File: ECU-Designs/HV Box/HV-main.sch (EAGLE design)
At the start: 57 parts, among them IC2 MCP6002, IC3 MCP6002, T1 120, T2 120

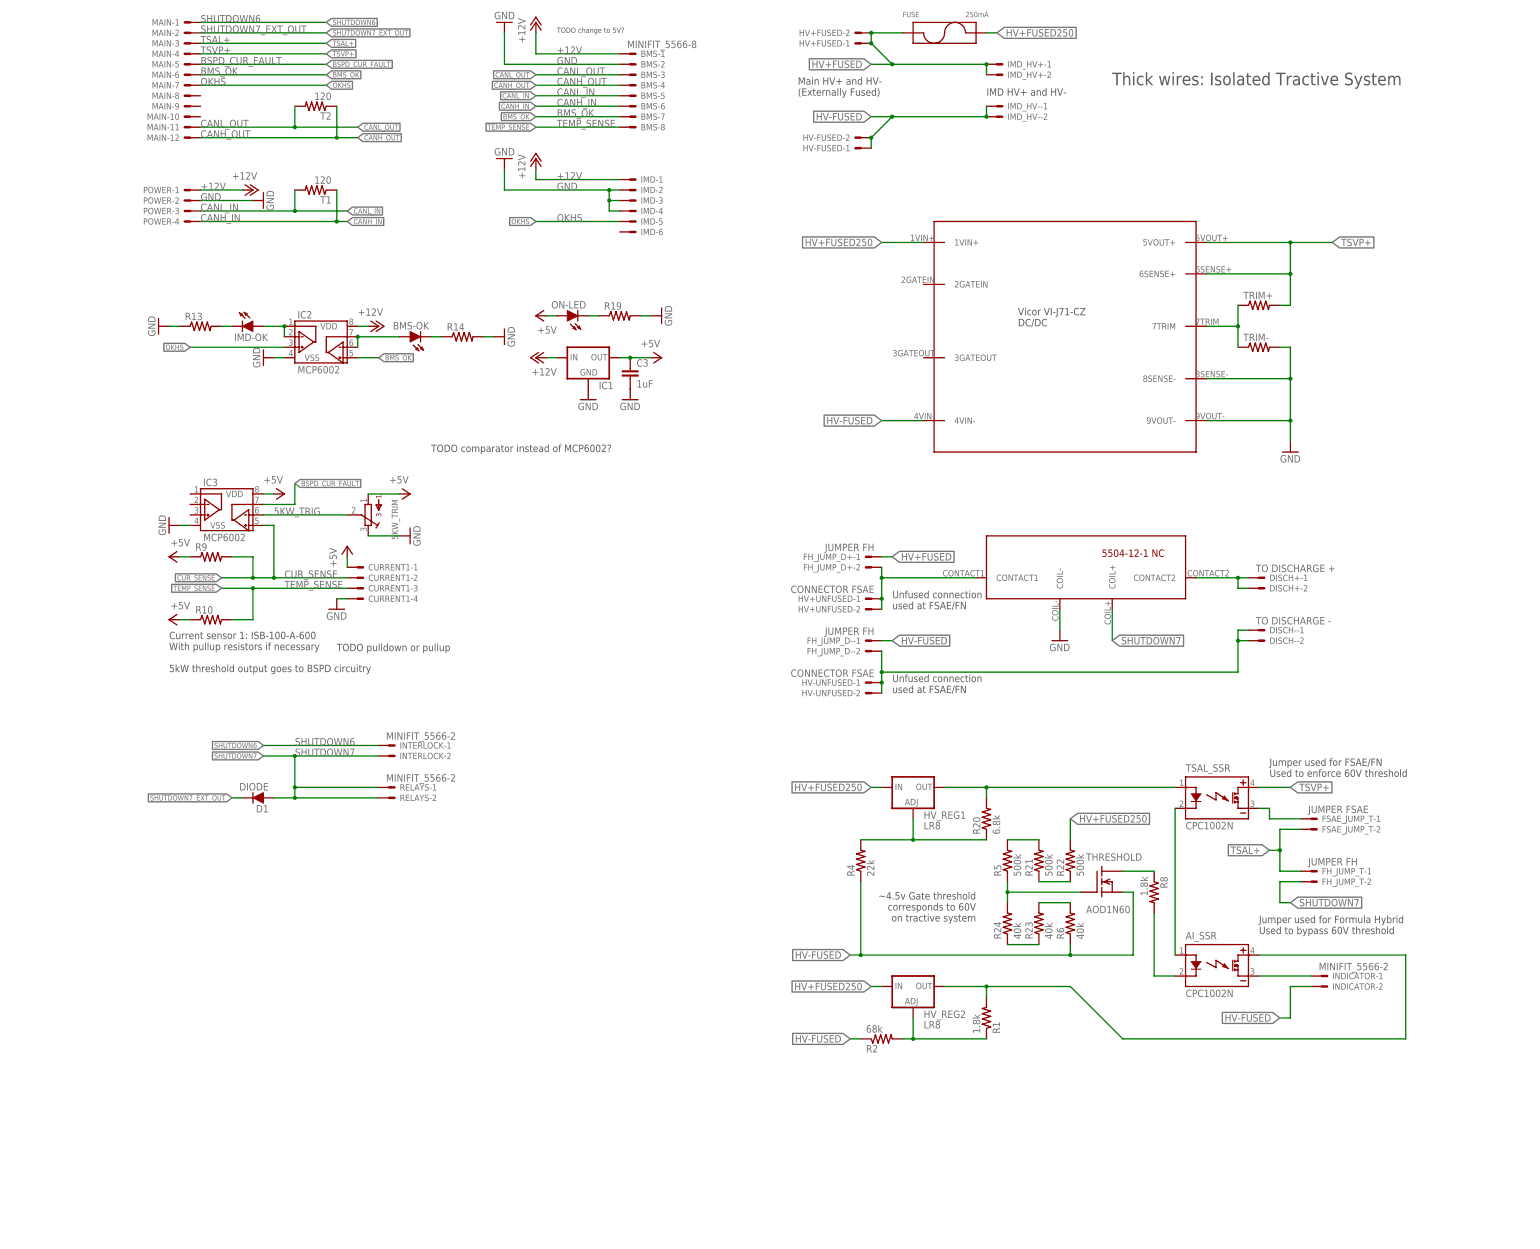
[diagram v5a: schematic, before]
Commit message: Change BSPD to use MCP6002 as comparator, HV board more resistors to meet voltage ratings
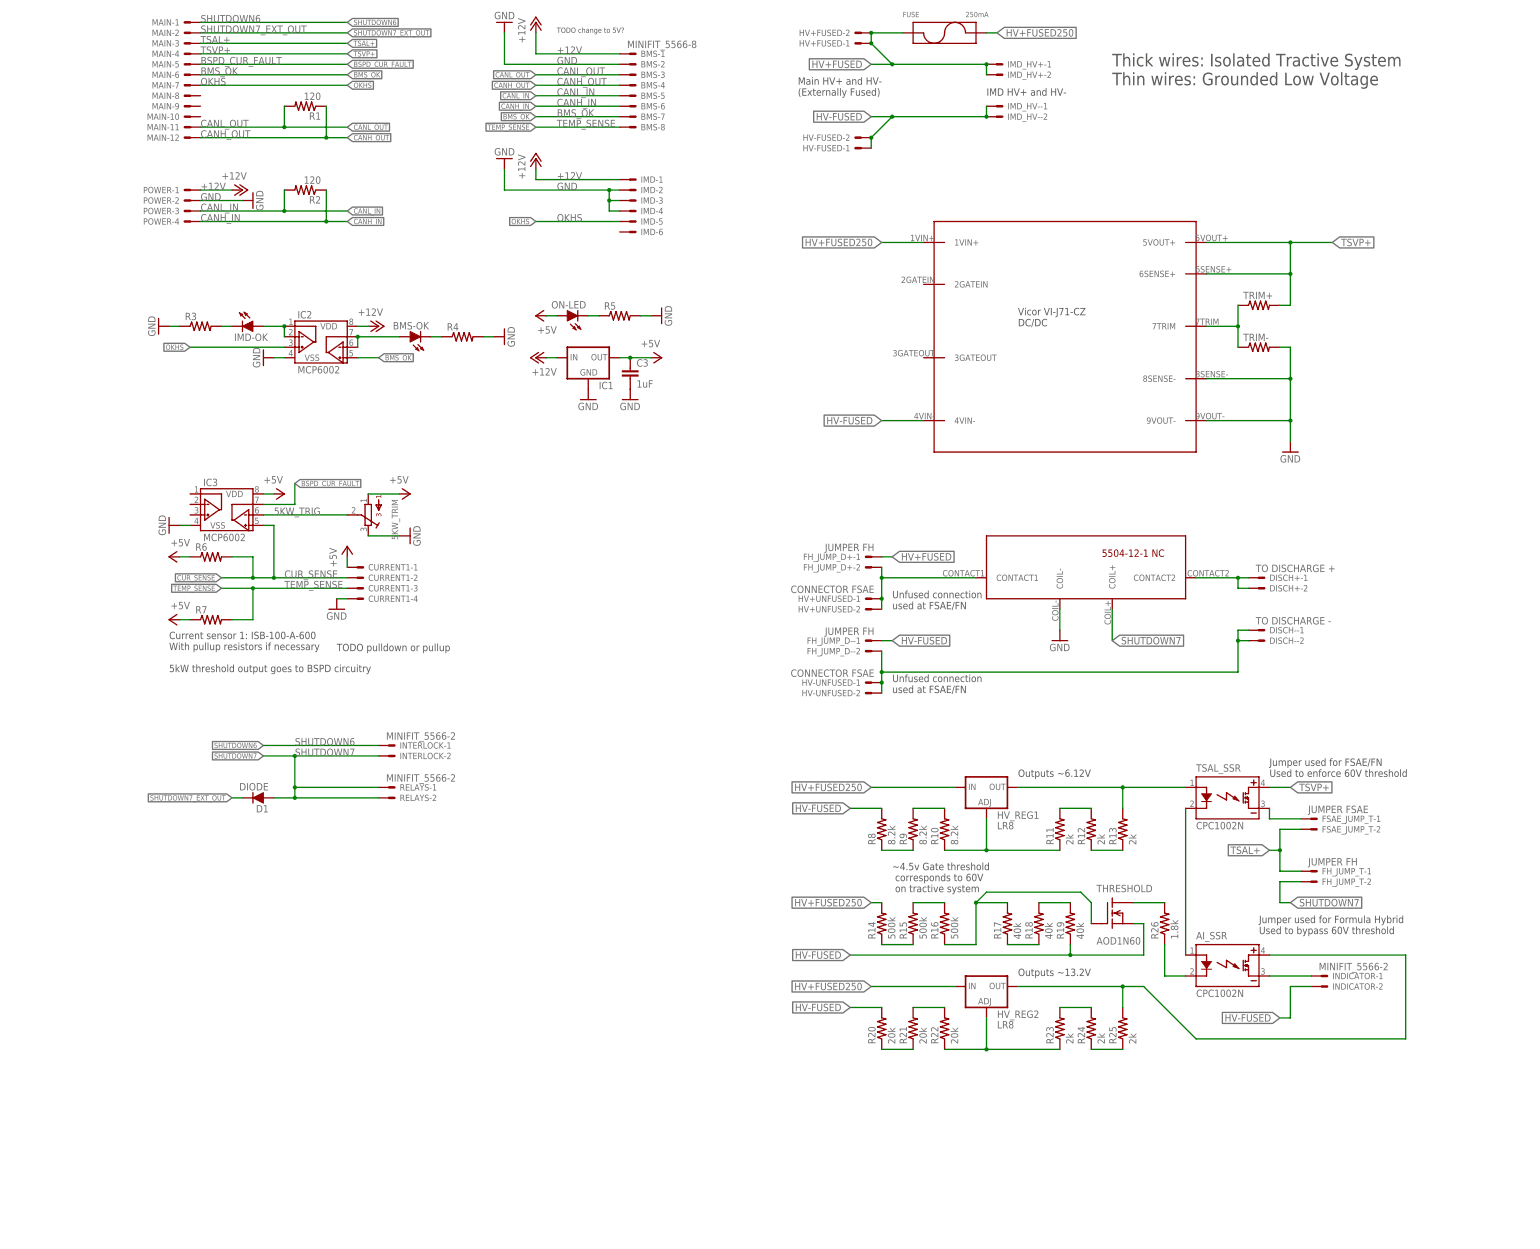
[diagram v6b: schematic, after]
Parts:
- removed T1, T2: 120, HyTechDevices:RESISTOR0805-RES
- added R11, R12, R25: 2k, HyTechDevices:RESISTOR0805-RES
- added R15, R16: 500k, HyTechDevices:RESISTOR0805-RES
- added R17, R18: 40k, HyTechDevices:RESISTOR0805-RES
- added R26: 1.8k, HyTechDevices:RESISTOR0805-RES
- added R3, R7: (no value), HyTechDevices:RESISTOR0805-RES
- R1: value 1.8k -> 120
- R10, R9: value (none) -> 8.2k
- R13: value (none) -> 2k
- R14: value (none) -> 500k
- R19: value (none) -> 40k
- R2: value 68k -> 120
- R20: value 6.8k -> 20k
- R21, R22: value 500k -> 20k
- R23, R24: value 40k -> 2k
- R4: value 22k -> (none)
- R5: value 500k -> (none)
- R6: value 40k -> (none)
- R8: value 1.8k -> 8.2k
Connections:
- removed net N$35: R8.1, THRESHOLD.D
- removed net N$36: R24.2, R5.1, THRESHOLD.G
- new net N$14: R10.2, R9.2
- new net N$16: R11.2, R12.2
- new net N$17: R12.1, R13.1
- new net N$18: HV_REG1.ADJ, R10.1, R11.1
- new net N$19: R23.2, R24.2
- new net N$20: R24.1, R25.1
- new net N$21: R21.2, R22.2
- new net N$22: R16.1, R17.2, THRESHOLD.G
- new net N$23: R20.1, R21.1
- new net N$8: R8.1, R9.1
- net +5V: now also R6.1, R7.1; no longer R10.1, R9.1
- net CANH_IN: now also R2.1; no longer T1.1
- net CANH_OUT: now also R1.1; no longer T2.1
- net CANL_IN: now also R2.2; no longer T1.2
- net CANL_OUT: now also R1.2; no longer T2.2
- net CUR_SENSE: now also R6.2; no longer R9.2
- net GND: now also R3.1, R4.2, R5.2; no longer R13.1, R14.2, R19.2
- net HV+FUSED250: now also R14.2; no longer R22.2
- net HV-FUSED: now also R19.1, R20.2, R8.2; no longer R2.1, R4.1, R6.1
- net N$1: now also R25.2; no longer R1.2
- net N$10: now also R14.1, R15.1; no longer R21.1, R22.1
- net N$11: now also R15.2, R16.2; no longer R21.2, R5.2
- net N$12: now also R17.1, R18.1; no longer R23.1, R24.1
- net N$13: now also R18.2, R19.2; no longer R23.2, R6.2
- net N$15: now also R22.1, R23.1; no longer R1.1, R2.2
- net N$2: now also R13.2; no longer R20.2
- net N$3: now also R5.1; no longer R19.1
- net N$44: now also R4.1; no longer R14.1
- net N$45: now also R3.2; no longer R13.2
- net N$5: now also R26.1; no longer R8.2
- net N$9: now also R26.2, THRESHOLD.D; no longer HV_REG1.ADJ, R20.1, R4.2
- net TEMP_SENSE: now also R7.2; no longer R10.2
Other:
- note added: "Outputs ~13.2V"
- note added: "Outputs ~6.12V"
- note added: "Thick wires: Isolated Tractive System Thin wires: Grounded Low Voltage"
- note removed: "TODO comparator instead of MCP6002?"
- note removed: "Thick wires: Isolated Tractive System"
- moved on the sheet: AI_SSR, HV_REG1, HV_REG2, R1, R10, R13, R14, R19, R2, R20, R21, R22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

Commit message: Progress on HV board, single 250mA fuse
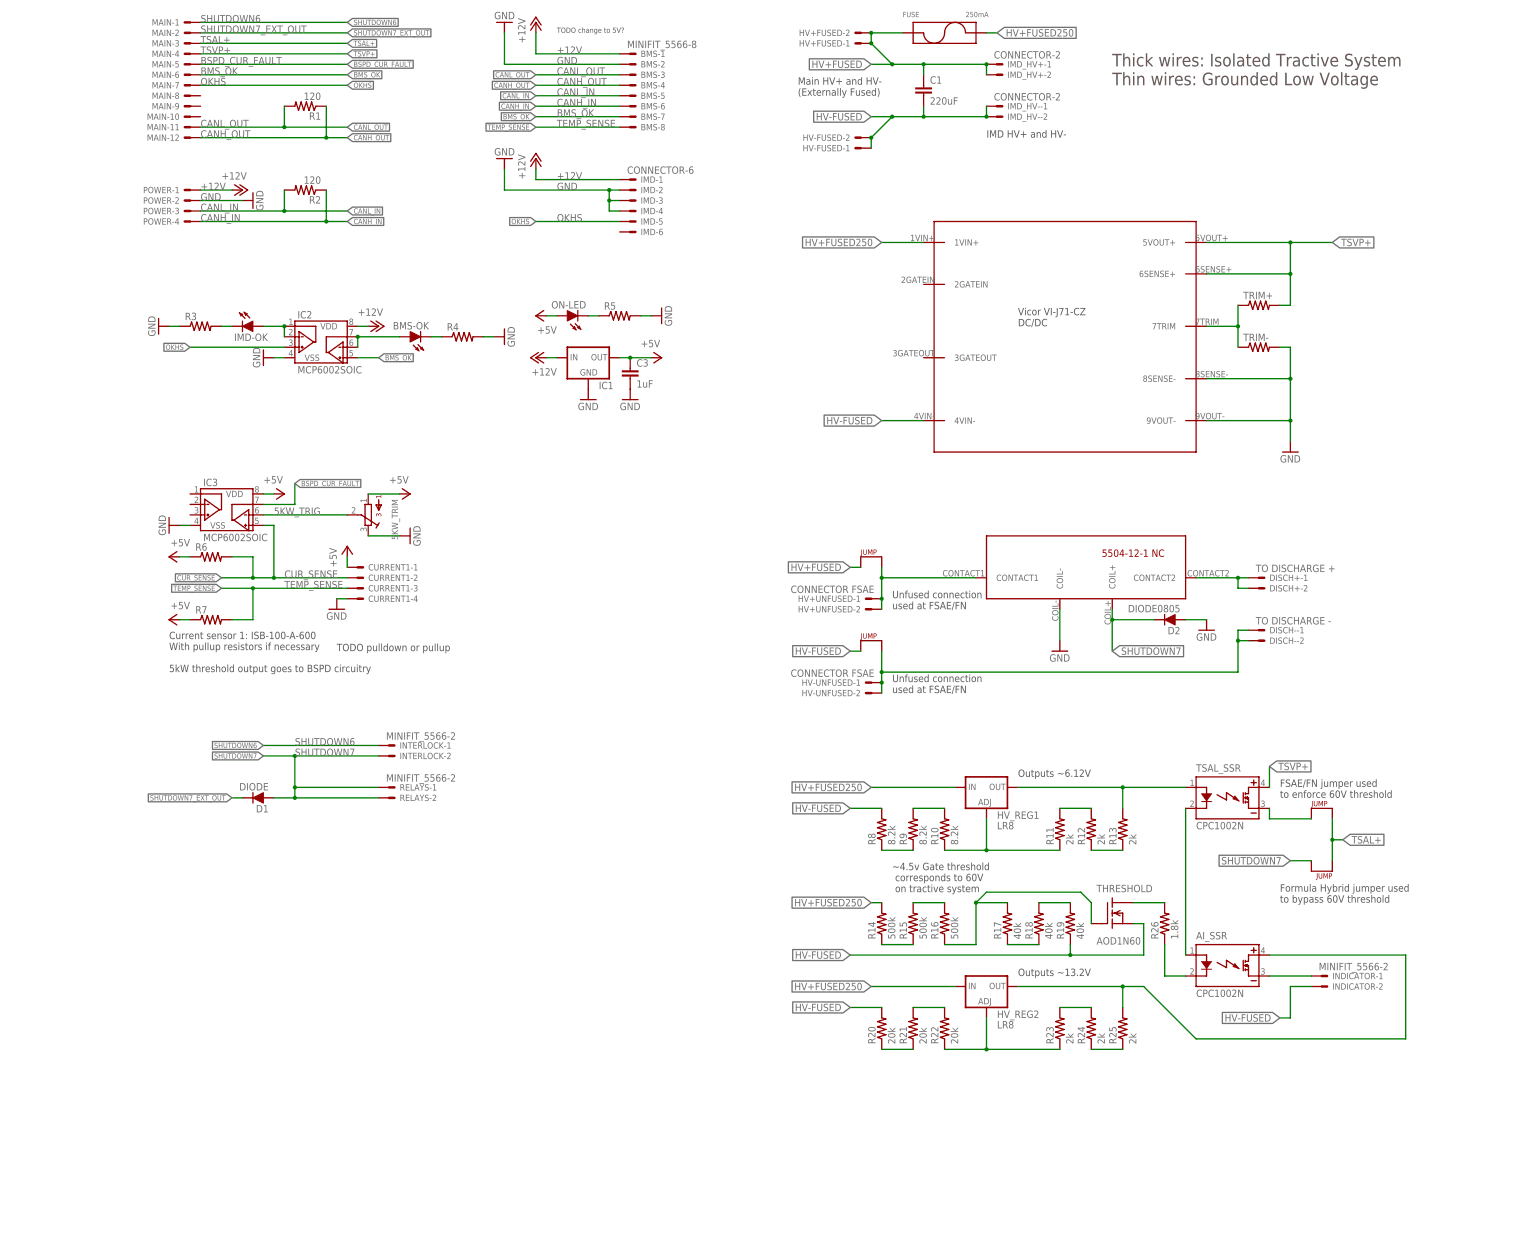
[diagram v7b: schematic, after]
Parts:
- removed FH_JUMP_D+, FH_JUMP_D-: JUMPER FH, HyTechDevices:CONNECTOR-2
- removed FH_JUMP_T: JUMPER FH, HyTechDevices:MINIFIT_5566-2
- removed FSAE_JUMP_T: JUMPER FSAE, HyTechDevices:MINIFIT_5566-2
- added C1: 220uF, HyTechDevices:CAP
- added D2: DIODE0805, HyTechDevices:DIODE0805
- added U$1, U$2, U$3, U$4: JUMPER.3, HyTechDevices:JUMPER.3
- IC2, IC3: value MCP6002 -> MCP6002SOIC; device HyTechDevices:MCP6002 -> HyTechDevices:MCP6002SOIC
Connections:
- net DISCHARGE1: now also U$3.P$2; no longer FH_JUMP_D+-2.S
- net DISCHARGE3: now also U$4.P$2; no longer FH_JUMP_D--2.S
- net GND: now also D2.A
- net HV+FUSED: now also C1.1, U$3.P$1; no longer FH_JUMP_D+-1.S
- net HV-FUSED: now also C1.2, U$4.P$1; no longer FH_JUMP_D--1.S
- net N$4: now also U$1.P$1; no longer FSAE_JUMP_T-1.S
- net SHUTDOWN7: now also D2.C, U$2.P$2; no longer FH_JUMP_T-2.S
- net TSAL+: now also U$1.P$2, U$2.P$1; no longer FH_JUMP_T-1.S, FSAE_JUMP_T-2.S
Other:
- note added: "FSAE/FN jumper used to enforce 60V threshold"
- note added: "Formula Hybrid jumper used to bypass 60V threshold"
- note removed: "Jumper used for FSAE/FN Used to enforce 60V threshold"
- note removed: "Jumper used for Formula Hybrid Used to bypass 60V threshold"
